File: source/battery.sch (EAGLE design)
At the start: 21 parts, among them SW1 SWITCH, U1 TP5410

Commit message: Update source to v11 of the project
Minor updates.
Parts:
- BAT+, U$5: device battery:PIN -> alim:PIN
- C1, C2, C3, C4: device battery:C22U -> alim:C22U
- C5, C6: device battery:C100N -> alim:C100N
- D1: device battery:SS32 -> alim:SS32
- I1: device battery:IND47M -> alim:IND47M
- LD1: device battery:LEDBI -> alim:LEDBI
- LD2: device battery:LED_POWER -> alim:LED_POWER
- R1: device battery:R293K -> alim:R293K
- R2: device battery:R0.3 -> alim:R0.3
- R3: device battery:R1K -> alim:R1K
- R5: device battery:R680 -> alim:R680
- SW1: device battery:SWITCH -> alim:SWITCH
- U$1: device battery:USB20 -> alim:USB20
- U$3: device battery:MICRO-USB -> alim:MICRO-USB
- U1: device battery:TP5410 -> alim:TP5410
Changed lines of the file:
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@@
 </classes>
 <parts>
-<part name="U1" library="battery" deviceset="TP5410" device=""/>
-<part name="D1" library="battery" deviceset="SS32" device=""/>
-<part name="I1" library="battery" deviceset="IND47M" device=""/>
-<part name="C1" library="battery" deviceset="C22U" device=""/>
-<part name="C2" library="battery" deviceset="C22U" device=""/>
-<part name="C3" library="battery" deviceset="C22U" device=""/>
-<part name="C4" library="battery" deviceset="C22U" device=""/>
-<part name="GND2" library="battery" deviceset="GND" device=""/>
-<part name="GND4" library="battery" deviceset="GND" device=""/>
-<part name="GND5" library="battery" deviceset="GND" device=""/>
-<part name="GND6" library="battery" deviceset="GND" device=""/>
-<part name="GND7" library="battery" deviceset="GND" device=""/>
-<part name="R3" library="battery" deviceset="R1K" device=""/>
-<part name="R5" library="battery" deviceset="R680" device="" value="R4.7K"/>
-<part name="U$3" library="battery" deviceset="MICRO-USB" device=""/>
-<part name="BAT+" library="battery" deviceset="PIN" device=""/>
-<part name="U$5" library="battery" deviceset="PIN" device=""/>
-<part name="GND1" library="battery" deviceset="GND" device=""/>
-<part name="GND3" library="battery" deviceset="GND" device=""/>
-<part name="GND8" library="battery" deviceset="GND" device=""/>
-<part name="C5" library="battery" deviceset="C100N" device=""/>
-<part name="GND9" library="battery" deviceset="GND" device=""/>
-<part name="C6" library="battery" deviceset="C100N" device=""/>
-<part name="GND10" library="battery" deviceset="GND" device=""/>
-<part name="U$1" library="battery" deviceset="USB20" device=""/>
-<part name="GND11" library="battery" deviceset="GND" device=""/>
-<part name="R1" library="battery" deviceset="R293K" device=""/>
+<part name="U1" library="alim" deviceset="TP5410" device=""/>
+<part name="D1" library="alim" deviceset="SS32" device=""/>
+<part name="I1" library="alim" deviceset="IND47M" device=""/>
+<part name="C1" library="alim" deviceset="C22U" device=""/>
+<part name="C2" library="alim" deviceset="C22U" device=""/>
+<part name="C3" library="alim" deviceset="C22U" device=""/>
+<part name="C4" library="alim" deviceset="C22U" device=""/>
+<part name="GND2" library="alim" deviceset="GND" device=""/>
+<part name="GND4" library="alim" deviceset="GND" device=""/>
+<part name="GND5" library="alim" deviceset="GND" device=""/>
+<part name="GND6" library="alim" deviceset="GND" device=""/>
+<part name="GND7" library="alim" deviceset="GND" device=""/>
+<part name="R3" library="alim" deviceset="R1K" device=""/>
+<part name="R5" library="alim" deviceset="R680" device="" value="R4.7K"/>
+<part name="U$3" library="alim" deviceset="MICRO-USB" device=""/>
+<part name="BAT+" library="alim" deviceset="PIN" device=""/>
+<part name="U$5" library="alim" deviceset="PIN" device=""/>
+<part name="GND1" library="alim" deviceset="GND" device=""/>
+<part name="GND3" library="alim" deviceset="GND" device=""/>
+<part name="GND8" library="alim" deviceset="GND" device=""/>
+<part name="C5" library="alim" deviceset="C100N" device=""/>
+<part name="GND9" library="alim" deviceset="GND" device=""/>
+<part name="C6" library="alim" deviceset="C100N" device=""/>
+<part name="GND10" library="alim" deviceset="GND" device=""/>
+<part name="U$1" library="alim" deviceset="USB20" device=""/>
+<part name="GND11" library="alim" deviceset="GND" device=""/>
+<part name="R1" library="alim" deviceset="R293K" device=""/>
 <part name="C7" library="rcl" deviceset="C-EU" device="C0603K"/>
-<part name="GND12" library="battery" deviceset="GND" device=""/>
-<part name="LD1" library="battery" deviceset="LEDBI" device=""/>
-<part name="P+1" library="battery" deviceset="VCC" device=""/>
-<part name="P+2" library="battery" deviceset="VCC" device=""/>
-<part name="P+3" library="battery" deviceset="VCC" device=""/>
-<part name="P+4" library="battery" deviceset="VCC" device=""/>
-<part name="LD2" library="battery" deviceset="LED_POWER" device=""/>
-<part name="SW1" library="battery" deviceset="SWITCH" device="" value="SWITCH"/>
-<part name="P+5" library="battery" deviceset="+5V" device=""/>
-<part name="GND13" library="battery" deviceset="GND" device=""/>
-<part name="P+6" library="battery" deviceset="+5V" device=""/>
-<part name="R2" library="battery" deviceset="R0.3" device="" value="R39"/>
+<part name="GND12" library="alim" deviceset="GND" device=""/>
+<part name="LD1" library="alim" deviceset="LEDBI" device=""/>
+<part name="P+1" library="alim" deviceset="VCC" device=""/>
+<part name="P+2" library="alim" deviceset="VCC" device=""/>
+<part name="P+3" library="alim" deviceset="VCC" device=""/>
+<part name="P+4" library="alim" deviceset="VCC" device=""/>
+<part name="LD2" library="alim" deviceset="LED_POWER" device=""/>
+<part name="SW1" library="alim" deviceset="SWITCH" device="" value="SWITCH"/>
+<part name="P+5" library="alim" deviceset="+5V" device=""/>
+<part name="GND13" library="alim" deviceset="GND" device=""/>
+<part name="P+6" library="alim" deviceset="+5V" device=""/>
+<part name="R2" library="alim" deviceset="R0.3" device="" value="R39"/>
 </parts>
 <sheets>

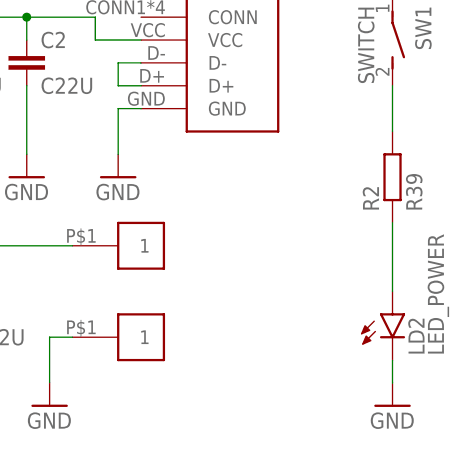
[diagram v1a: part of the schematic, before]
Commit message: Update to v12 of the project
This slightly rearranges certain tracks to ease laser engraving,
manual components placement and soldering.
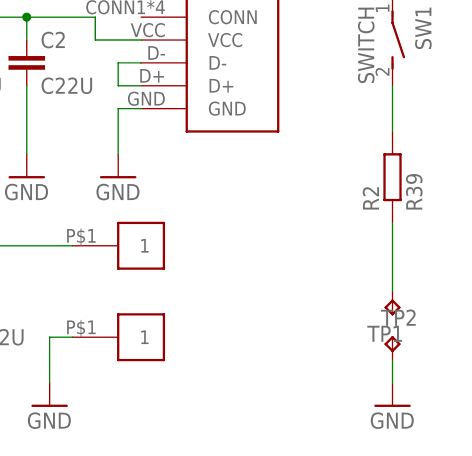
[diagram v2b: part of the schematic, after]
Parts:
- removed LD2: LED_POWER, alim:LED_POWER
- added TP1, TP2: TPB1,27, testpad:TPB1,27
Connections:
- net GND: now also TP2.TP; no longer LD2.C
- net N$3: now also TP1.TP; no longer LD2.A
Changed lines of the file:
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@@
 <?xml version="1.0" encoding="utf-8"?>
 <!DOCTYPE eagle SYSTEM "eagle.dtd">
-<eagle version="7.6.0">
+<eagle version="7.7.0">
 <drawing>
 <settings>
@@
 <part name="P+3" library="alim" deviceset="VCC" device=""/>
 <part name="P+4" library="alim" deviceset="VCC" device=""/>
-<part name="LD2" library="alim" deviceset="LED_POWER" device=""/>
 <part name="SW1" library="alim" deviceset="SWITCH" device="" value="SWITCH"/>
 <part name="P+5" library="alim" deviceset="+5V" device=""/>
@@
 <part name="P+6" library="alim" deviceset="+5V" device=""/>
 <part name="R2" library="alim" deviceset="R0.3" device="" value="R39"/>
+<part name="TP1" library="testpad" deviceset="TP" device="B1,27"/>
+<part name="TP2" library="testpad" deviceset="TP" device="B1,27"/>
 </parts>
 <sheets>
@@
 <attribute name="VALUE" x="53.34" y="63.5" size="1.778" layer="96" rot="R90"/>
 </instance>
-<instance part="LD2" gate="G$1" x="185.42" y="15.24" smashed="yes">
-<attribute name="NAME" x="188.976" y="10.668" size="1.778" layer="95" rot="R90"/>
-<attribute name="VALUE" x="191.135" y="10.668" size="1.778" layer="96" rot="R90"/>
-</instance>
 <instance part="SW1" gate="G$1" x="185.42" y="45.72" smashed="yes" rot="R180">
 <attribute name="NAME" x="187.96" y="49.53" size="1.778" layer="95" rot="R270"/>
@@
 <attribute name="VALUE" x="188.722" y="26.67" size="1.778" layer="96" rot="R90"/>
 </instance>
+<instance part="TP1" gate="G$1" x="185.42" y="15.24" rot="R180"/>
+<instance part="TP2" gate="G$1" x="185.42" y="12.7"/>
 </instances>
 <busses>
@@
 </segment>
 <segment>
-<pinref part="LD2" gate="G$1" pin="C"/>
 <pinref part="GND13" gate="1" pin="GND"/>
 <wire x1="185.42" y1="10.16" x2="185.42" y2="7.62" width="0.1524" layer="91"/>
+<pinref part="TP2" gate="G$1" pin="TP"/>
 </segment>
 </net>
@@
 <segment>
 <pinref part="R2" gate="G$1" pin="1"/>
-<pinref part="LD2" gate="G$1" pin="A"/>
 <wire x1="185.42" y1="25.4" x2="185.42" y2="17.78" width="0.1524" layer="91"/>
-</segment>
-</net>
+<pinref part="TP1" gate="G$1" pin="TP"/>
+</segment>
+</net>
